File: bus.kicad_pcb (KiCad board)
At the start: 2 copper layers, 111.8 x 48.3 mm, 26 parts, among them J1 CONN_02X08, J12 Screw_Terminal_1x04, J2 CONN_02X08, J3 CONN_02X08, J4 CONN_02X08, J5 CONN_02X08, J6 CONN_02X08, J7 CONN_02X08, J8 CONN_02X08, J9 CONN_02X08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

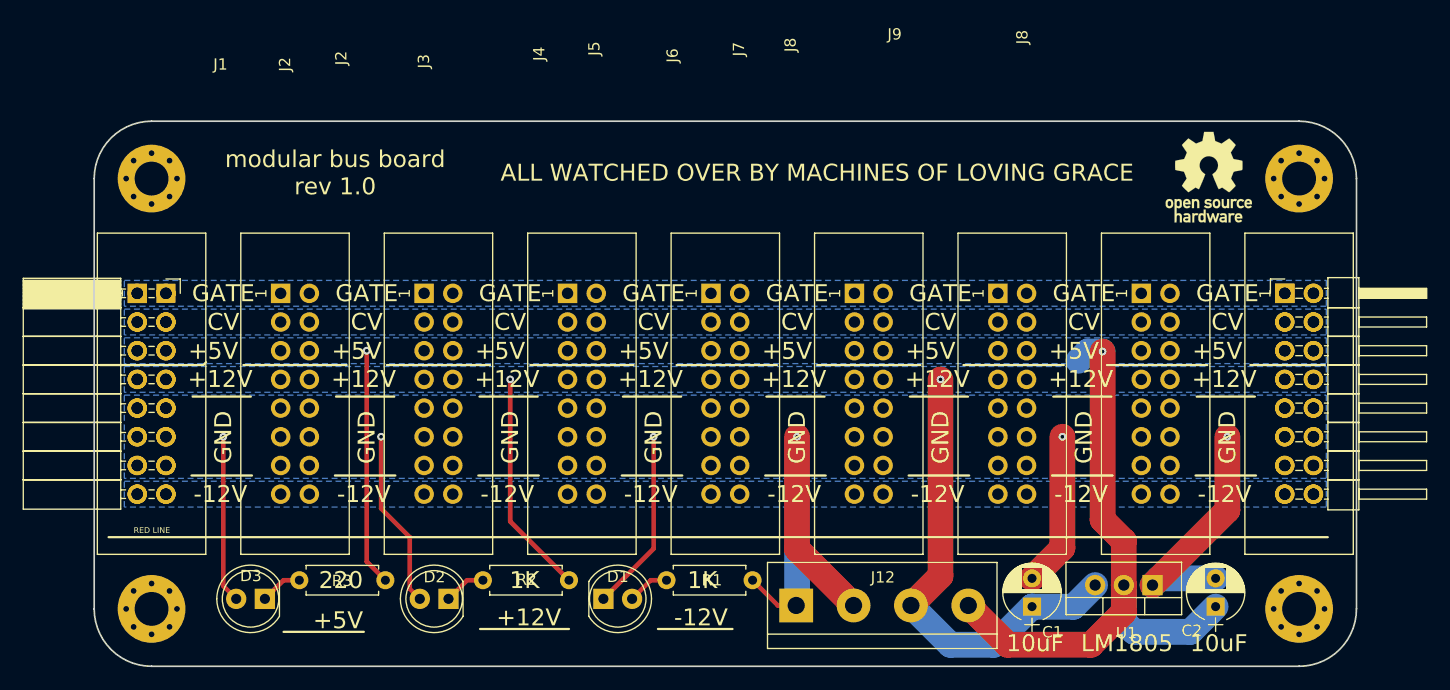
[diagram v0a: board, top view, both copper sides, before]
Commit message: Moved LM1085 and silkscreen label clean-up
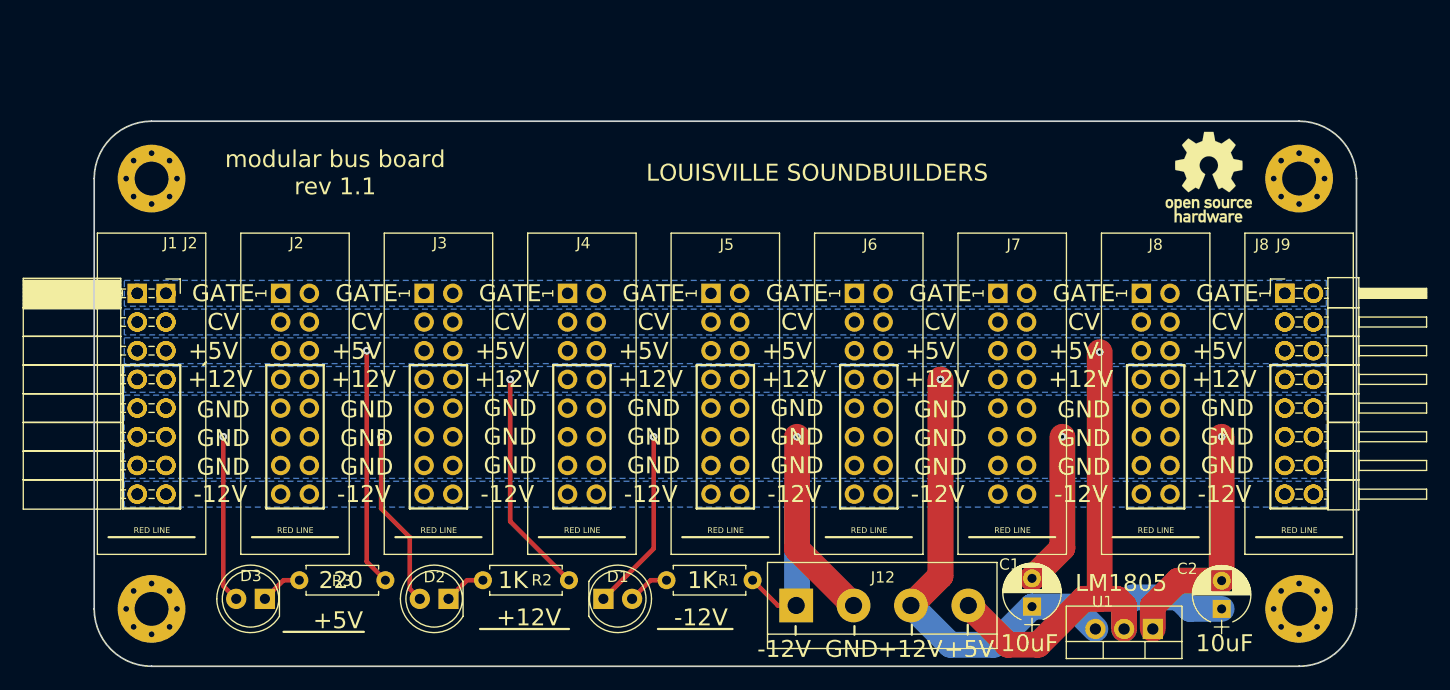
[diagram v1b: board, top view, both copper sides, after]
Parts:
- moved U1 3.89 mm to (159.8, 105.9)
- moved C2 0.57 mm to (165.9, 104.1)
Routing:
- net +5V: track 76.4 -> 73.5 mm
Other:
- board text added: "LOUISVILLE SOUNDBUILDERS"
- board text added: "modular bus board rev 1.1"
- board text removed: "ALL WATCHED OVER BY MACHINES OF LOVING GRACE"
- board text removed: "modular bus board rev 1.0"
